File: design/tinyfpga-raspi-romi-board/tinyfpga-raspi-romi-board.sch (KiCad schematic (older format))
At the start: 32 parts, among them J1 TINYFPGA_J1, J10 ROMI_ENC_LEFT, J11 ROMI_ENC_RIGHT, J12 QTR_LEFT, J13 QTR_RIGHT, J14 SONAR_LEFT, J15 SONAR_RIGHT, J16 PWR_SEL1, J17 PWR_SEL0, J2 TINYFPGA_J2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

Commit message: added leds and user buttons. needs to be refactored to more sheets
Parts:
- added D? (x8): LED, symbol Device:LED
- added Q? (x8): 2N7000, Package_TO_SOT_THT:TO-92_Inline, symbol Transistor_FET:2N7000
- added R? (x19): 1k, Resistor_THT:R_Axial_DIN0204_L3.6mm_D1.6mm_P1.90mm_Vertical, symbol Device:R_US
- added SW? (x3): SW_Push, symbol Switch:SW_Push
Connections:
- net labels added: FPGA_BTN0, FPGA_BTN1, FPGA_BTN_RST, FPGA_LED0, FPGA_LED1, FPGA_LED2, FPGA_LED3, FPGA_LED4, FPGA_LED5, FPGA_LED6, FPGA_LED7
- wire segments 202 -> 324
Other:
- note added: "User Buttons"
- note added: "User LEDs"
- moved on the sheet: C1, D1, F1, J1, J10, J11, J12, J13, J16, J17, J2, J4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

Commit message: cluttered and gross... JUST THE WAY I LIKE IT
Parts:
- removed R3, R5, R6, R7, R8, R? (x19): 1k, Resistor_THT:R_Axial_DIN0204_L3.6mm_D1.6mm_P1.90mm_Vertical, symbol Device:R_US
- added J?: Conn_02x09_Odd_Even, symbol Connector_Generic:Conn_02x09_Odd_Even
- added R? (x6): 3.9k, Resistor_THT:R_Axial_DIN0204_L3.6mm_D1.6mm_P1.90mm_Vertical, symbol Device:R_US
- added R? (x16): 268, Resistor_THT:R_Axial_DIN0204_L3.6mm_D1.6mm_P1.90mm_Vertical, symbol Device:R_US
- C1: value 10uF -> 47uF
- F1: value MF-MSMF250/X -> MF-MSMF250/16X-2
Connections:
- net labels added: RPI_GPIO12, RPI_GPIO13, RPI_GPIO16, RPI_GPIO17, RPI_GPIO18, RPI_GPIO19, RPI_GPIO2, RPI_GPIO20, RPI_GPIO21, RPI_GPIO22, RPI_GPIO23, RPI_GPIO24, RPI_GPIO25, RPI_GPIO26, RPI_GPIO27, RPI_GPIO3, RPI_GPIO4, RPI_GPIO7
- net labels removed: FPGA_110, FPGA_112, FPGA_140, FPGA_185, FPGA_221, FPGA_224, FPGA_24B, FPGA_3A, FPGA_56, FPGA_57, FPGA_70
- wire segments 324 -> 358
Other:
- note added: "Sonar is 5V I/O but 3.3V is\nenough to assert TRIG, and the\nECHO can be read with a simple\nvoltage divider. 2.5V will register\nas HIGH."
- note added: "TinyFPGA I/O Headers"
- note removed: "Sonar is 5V I/O but 3.3V is enough to\nassert TRIG, and the ECHO can be read\nwith a simple voltage divider.\n\nTwo 1k resistors are used to reduce unique\npart count."
- moved on the sheet: C1, D1, D?, F1, J10, J11, J12, J13, J14, J15, J3, J6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

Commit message: finally got footprints on a board. starting arranging them
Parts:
- removed J12: QTR_LEFT, symbol Connector:Conn_01x04_Female
- removed J13: QTR_RIGHT, symbol Connector:Conn_01x04_Female
- added C2: 1uF, Capacitor_THT:C_Rect_L4.0mm_W2.5mm_P2.50mm, symbol Device:C
- added J12: QTR_LEFT, Connector_PinSocket_2.54mm:PinSocket_2x02_P2.54mm_Vertical, symbol Connector_Generic:Conn_02x02_Odd_Even
- added J13: QTR_RIGHT, Connector_PinSocket_2.54mm:PinSocket_2x02_P2.54mm_Vertical, symbol Connector_Generic:Conn_02x02_Odd_Even
- added J19: ON_OFF, Connector_PinHeader_1.27mm:PinHeader_1x02_P1.27mm_Vertical, symbol Connector:Conn_01x02_Male
- added J20: ROMI_POWER, Connector_PinHeader_2.54mm:PinHeader_2x05_P2.54mm_Vertical, symbol Connector_Generic:Conn_02x05_Odd_Even
- C1: value 47uF -> 22uF; footprint (none) -> Capacitor_THT:CP_Radial_D5.0mm_P2.00mm
- D1: footprint (none) -> Diode_SMD:D_SMB_Handsoldering; Datasheet (none) -> https://media.digikey.com/pdf/Data%20Sheets/Littelfuse%20PD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
- D2, D3, D4, D5, D6, D7, D8, D9: renamed from D?; footprint (none) -> LED_THT:LED_D5.0mm_Clear
- F1: footprint (none) -> Fuse:Fuse_1812_4532Metric_Pad1.30x3.40mm_HandSolder
- J1, J2: footprint (none) -> Connector_PinSocket_2.54mm:PinSocket_1x14_P2.54mm_Vertical
- J10, J11: footprint (none) -> Connector_PinSocket_2.54mm:PinSocket_1x03_P2.54mm_Vertical
- J14, J15: footprint (none) -> Connector_PinHeader_2.54mm:PinHeader_1x04_P2.54mm_Vertical
- J16, J17: footprint (none) -> Connector_PinHeader_2.54mm:PinHeader_1x03_P2.54mm_Vertical
- J18: renamed from J?; value Conn_02x09_Odd_Even -> RPI_EXTRA; footprint (none) -> Connector_PinHeader_2.54mm:PinHeader_2x09_P2.54mm_Vertical
- J3: footprint Connector_PinSocket_2.54mm:PinSocket_2x20_P2.54mm_Vertical -> Connector_PinSocket_2.54mm:PinSocket_2x20_P2.54mm_Horizontal
- J4: footprint (none) -> Connector_PinSocket_2.54mm:PinSocket_2x08_P2.54mm_Vertical
- J5, J7: footprint (none) -> Connector_PinSocket_2.54mm:PinSocket_2x03_P2.54mm_Vertical
- J9: footprint (none) -> Connector_PinHeader_2.54mm:PinHeader_1x06_P2.54mm_Vertical
- R1, R10, R2, R4, R9: footprint Resistor_THT:R_Axial_DIN0204_L3.6mm_D1.6mm_P1.90mm_Vertical -> Resistor_THT:R_Axial_DIN0204_L3.6mm_D1.6mm_P2.54mm_Vertical
- R11, R12, R13, R14, R15, R16, R17, R18, R19, R20, R21, R22, R23, R24, R25, R26, R27, R3, R5, R6, R7, R8: renamed from R?; footprint Resistor_THT:R_Axial_DIN0204_L3.6mm_D1.6mm_P1.90mm_Vertical -> Resistor_THT:R_Axial_DIN0204_L3.6mm_D1.6mm_P2.54mm_Vertical
- SW2, SW3, SW4: renamed from SW?; footprint (none) -> Button_Switch_THT:SW_PUSH_6mm_H5mm
- U1: footprint (none) -> Package_SO:SOIC-8_3.9x4.9mm_P1.27mm
- gave numbers to parts that had none: 8
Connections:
- net labels removed: ROMI_VSW
- wire segments 358 -> 378
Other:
- moved on the sheet: C1, D1, J3

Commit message: imported mech drawings to kicad pcb for placement
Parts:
- A1: symbol custom:OKR-T_3-W12-C -> tinyfpga-raspi-romi-board-rescue:OKR-T_3-W12-C-custom
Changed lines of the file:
@@
 EESchema Schematic File Version 4
+LIBS:tinyfpga-raspi-romi-board-cache
 EELAYER 29 0
 EELAYER END
@@
 	9800 3600 9200 3600
 $Comp
-L custom:OKR-T_3-W12-C A1
+L tinyfpga-raspi-romi-board-rescue:OKR-T_3-W12-C-custom A1
 U 1 1 5CD90422
 P 1950 2150

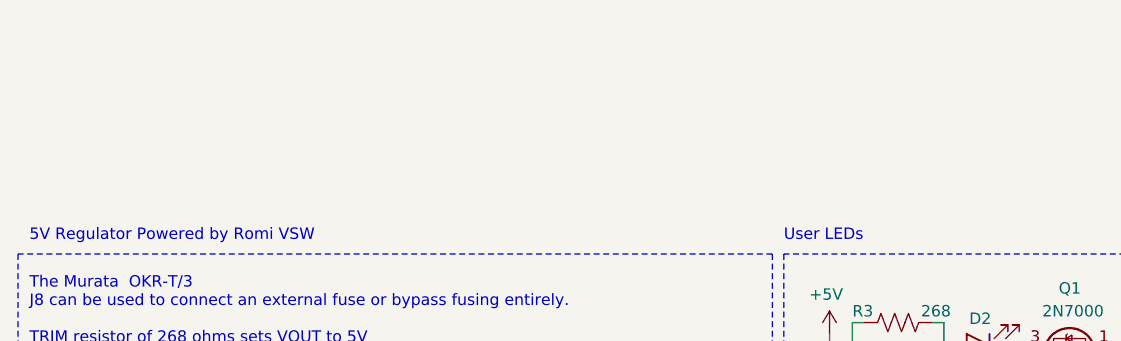
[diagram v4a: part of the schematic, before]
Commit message: made some minor tweaks and measured tinypcb with headers
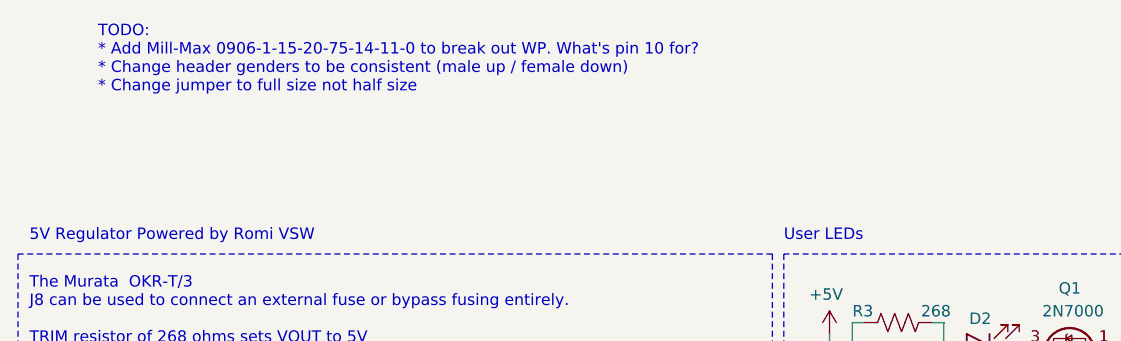
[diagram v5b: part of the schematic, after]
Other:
- note added: "TODO:\n* Add Mill-Max 0906-1-15-20-75-14-11-0 to break out WP. What's pin 10 for?\n* Change header genders to be consistent (male up / female down)\n* Change jumper to full size not half size"
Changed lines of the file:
@@
 Wire Wire Line
 	7450 1550 8050 1550
+Text Notes 900  -50  0    50   ~ 0
+TODO:\n* Add Mill-Max 0906-1-15-20-75-14-11-0 to break out WP. What's pin 10 for?\n* Change header genders to be consistent (male up / female down)\n* Change jumper to full size not half size
 $EndSCHEMATC

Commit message: Everything fits on a board
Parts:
- removed J18: RPI_EXTRA, Connector_PinHeader_2.54mm:PinHeader_2x09_P2.54mm_Vertical, symbol Connector_Generic:Conn_02x09_Odd_Even
- added J18: RPI_EXTRA, Connector_PinHeader_2.54mm:PinHeader_1x18_P2.54mm_Vertical, symbol Connector:Conn_01x18_Male
- J14: footprint Connector_PinHeader_2.54mm:PinHeader_1x04_P2.54mm_Vertical -> Connector_PinSocket_2.54mm:PinSocket_1x04_P2.54mm_Vertical
- J19, J6, J8: footprint Connector_PinHeader_1.27mm:PinHeader_1x02_P1.27mm_Vertical -> Connector_PinHeader_2.54mm:PinHeader_1x02_P2.54mm_Vertical
- J20: footprint Connector_PinHeader_2.54mm:PinHeader_2x05_P2.54mm_Vertical -> Connector_PinHeader_2.54mm:PinHeader_2x05_P2.54mm_Vertical_SMD
- J4: footprint Connector_PinSocket_2.54mm:PinSocket_2x08_P2.54mm_Vertical -> Connector_PinSocket_2.54mm:PinSocket_2x08_P2.54mm_Vertical_SMD
- J5, J7: footprint Connector_PinSocket_2.54mm:PinSocket_2x03_P2.54mm_Vertical -> Connector_PinSocket_2.54mm:PinSocket_2x03_P2.54mm_Vertical_SMD
- J9: footprint Connector_PinHeader_2.54mm:PinHeader_1x06_P2.54mm_Vertical -> Connector_PinHeader_2.54mm:PinHeader_1x06_P2.54mm_Vertical_SMD_Pin1Left; symbol Connector:Conn_01x06_Female -> Connector:Conn_01x06_Male
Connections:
- net RPI_GPIO12: now also J18.6 (Pin_6)
- net RPI_GPIO13: now also J18.5 (Pin_5)
- net RPI_GPIO16: now also J18.8 (Pin_8)
- net RPI_GPIO17: now also J18.7 (Pin_7)
- net RPI_GPIO18: now also J18.10 (Pin_10)
- net RPI_GPIO19: now also J18.9 (Pin_9)
- net RPI_GPIO2: now also J18.2 (Pin_2)
- net RPI_GPIO20: now also J18.12 (Pin_12)
- net RPI_GPIO21: now also J18.11 (Pin_11)
- net RPI_GPIO22: now also J18.14 (Pin_14)
- net RPI_GPIO23: now also J18.13 (Pin_13)
- net RPI_GPIO24: now also J18.15 (Pin_15)
- net RPI_GPIO25: now also J18.16 (Pin_16)
- net RPI_GPIO26: now also J18.17 (Pin_17)
- net RPI_GPIO27: now also J18.18 (Pin_18)
- net RPI_GPIO3: now also J18.1 (Pin_1)
- net RPI_GPIO4: now also J18.4 (Pin_4)
- net RPI_GPIO7: now also J18.3 (Pin_3)
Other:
- moved on the sheet: J12, J13, J14, J15, J20, R10, R23, R24, R9

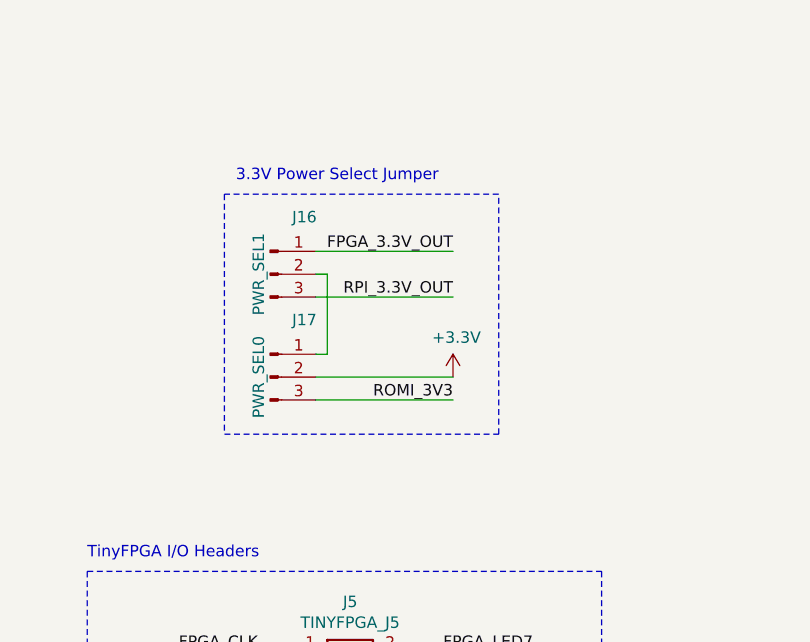
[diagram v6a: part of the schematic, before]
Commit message: All components placed on board. Needs routing doe
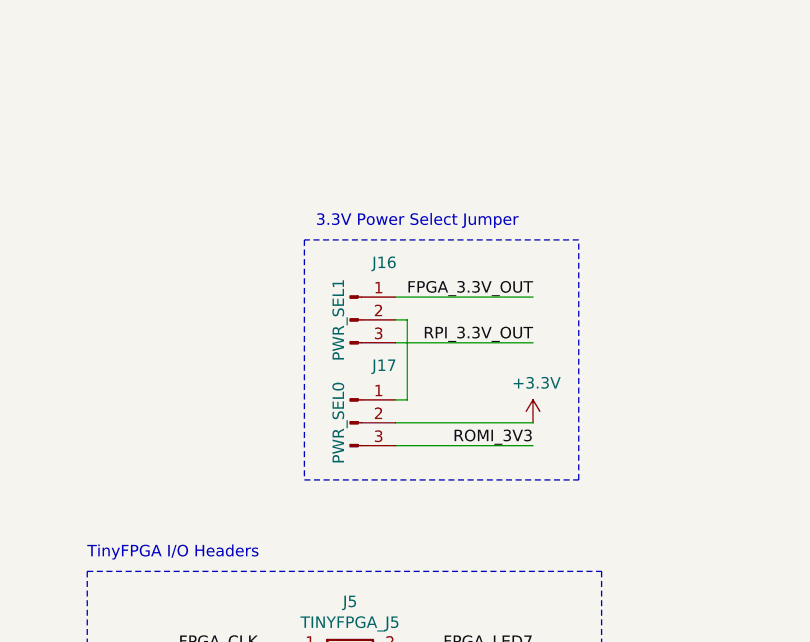
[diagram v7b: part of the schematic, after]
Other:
- moved on the sheet: J16, J17
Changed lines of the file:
@@
 L power:+3.3V #PWR029
 U 1 1 5D34863C
-P 10500 1550
-F 0 "#PWR029" H 10500 1400 50  0001 C CNN
-F 1 "+3.3V" H 10515 1723 50  0000 C CNN
-F 2 "" H 10500 1550 50  0001 C CNN
-F 3 "" H 10500 1550 50  0001 C CNN
-	1    10500 1550
+P 10850 1750
+F 0 "#PWR029" H 10850 1600 50  0001 C CNN
+F 1 "+3.3V" H 10865 1923 50  0000 C CNN
+F 2 "" H 10850 1750 50  0001 C CNN
+F 3 "" H 10850 1750 50  0001 C CNN
+	1    10850 1750
 	1    0    0    -1
 $EndComp
@@
 L Connector:Conn_01x03_Male J16
 U 1 1 5D3A31C2
-P 9700 1100
-F 0 "J16" H 9850 1350 50  0000 C CNN
-F 1 "PWR_SEL1" V 9650 1100 50  0000 C CNN
-F 2 "Connector_PinHeader_2.54mm:PinHeader_1x03_P2.54mm_Vertical" H 9700 1100 50  0001 C CNN
-F 3 "~" H 9700 1100 50  0001 C CNN
-	1    9700 1100
+P 10050 1300
+F 0 "J16" H 10200 1550 50  0000 C CNN
+F 1 "PWR_SEL1" V 10000 1300 50  0000 C CNN
+F 2 "Connector_PinHeader_2.54mm:PinHeader_1x03_P2.54mm_Vertical" H 10050 1300 50  0001 C CNN
+F 3 "~" H 10050 1300 50  0001 C CNN
+	1    10050 1300
 	1    0    0    -1
 $EndComp
-Text Label 10500 1200 2    50   ~ 0
+Text Label 10850 1400 2    50   ~ 0
 RPI_3.3V_OUT
-Text Label 10500 1000 2    50   ~ 0
+Text Label 10850 1200 2    50   ~ 0
 FPGA_3.3V_OUT
 Wire Wire Line
-	9900 1000 10500 1000
+	10250 1200 10850 1200
 Wire Wire Line
-	9900 1200 10500 1200
+	10250 1400 10850 1400
 Wire Wire Line
-	9950 1100 9950 1450
-Text Notes 9550 700  0    50   ~ 0
+	10300 1300 10300 1650
+Text Notes 9900 900  0    50   ~ 0
 3.3V Power Select Jumper
 $Comp
 L Connector:Conn_01x03_Male J17
 U 1 1 5D41FD53
-P 9700 1550
-F 0 "J17" H 9850 1800 50  0000 C CNN
-F 1 "PWR_SEL0" V 9650 1550 50  0000 C CNN
-F 2 "Connector_PinHeader_2.54mm:PinHeader_1x03_P2.54mm_Vertical" H 9700 1550 50  0001 C CNN
-F 3 "~" H 9700 1550 50  0001 C CNN
-	1    9700 1550
+P 10050 1750
+F 0 "J17" H 10200 2000 50  0000 C CNN
+F 1 "PWR_SEL0" V 10000 1750 50  0000 C CNN
+F 2 "Connector_PinHeader_2.54mm:PinHeader_1x03_P2.54mm_Vertical" H 10050 1750 50  0001 C CNN
+F 3 "~" H 10050 1750 50  0001 C CNN
+	1    10050 1750
 	1    0    0    -1
 $EndComp
-Text Label 10500 1650 2    50   ~ 0
+Text Label 10850 1850 2    50   ~ 0
 ROMI_3V3
 Wire Wire Line
-	10500 1550 9900 1550
+	10850 1750 10250 1750
 Wire Wire Line
-	9900 1450 9950 1450
+	10250 1650 10300 1650
 Wire Wire Line
-	9900 1650 10500 1650
+	10250 1850 10850 1850
 Wire Wire Line
-	9900 1100 9950 1100
+	10250 1300 10300 1300
 Wire Notes Line
-	9500 750  9500 1800
+	9850 950  9850 2000
 Wire Notes Line
-	9500 1800 10700 1800
+	9850 2000 11050 2000
 Wire Notes Line
-	10700 1800 10700 750
+	11050 2000 11050 950
 Wire Notes Line
-	10700 750  9500 750
+	11050 950  9850 950
 Wire Notes Line
 	8900 2400 11150 2400

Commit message: Spaced out componenets more
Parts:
- J15: footprint Connector_PinHeader_2.54mm:PinHeader_1x04_P2.54mm_Vertical -> Connector_PinSocket_2.54mm:PinSocket_1x04_P2.54mm_Vertical
- J7: footprint Connector_PinSocket_2.54mm:PinSocket_2x03_P2.54mm_Vertical_SMD -> Connector_PinHeader_2.54mm:PinHeader_2x03_P2.54mm_Vertical_SMD
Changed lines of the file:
@@
 F 0 "J15" H 14700 7050 50  0000 C CNN
 F 1 "SONAR_RIGHT" V 14700 6700 50  0000 C CNN
-F 2 "Connector_PinHeader_2.54mm:PinHeader_1x04_P2.54mm_Vertical" H 14650 6750 50  0001 C CNN
+F 2 "Connector_PinSocket_2.54mm:PinSocket_1x04_P2.54mm_Vertical" H 14650 6750 50  0001 C CNN
 F 3 "~" H 14650 6750 50  0001 C CNN
 	1    14650 6750
@@
 F 0 "J7" H 1100 2167 50  0000 C CNN
 F 1 "ROMI_VSW" H 1100 2076 50  0000 C CNN
-F 2 "Connector_PinSocket_2.54mm:PinSocket_2x03_P2.54mm_Vertical_SMD" H 1050 1850 50  0001 C CNN
+F 2 "Connector_PinHeader_2.54mm:PinHeader_2x03_P2.54mm_Vertical_SMD" H 1050 1850 50  0001 C CNN
 F 3 "~" H 1050 1850 50  0001 C CNN
 	1    1050 1850
